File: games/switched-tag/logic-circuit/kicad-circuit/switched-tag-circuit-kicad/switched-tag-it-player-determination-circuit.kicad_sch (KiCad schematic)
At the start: 16 parts

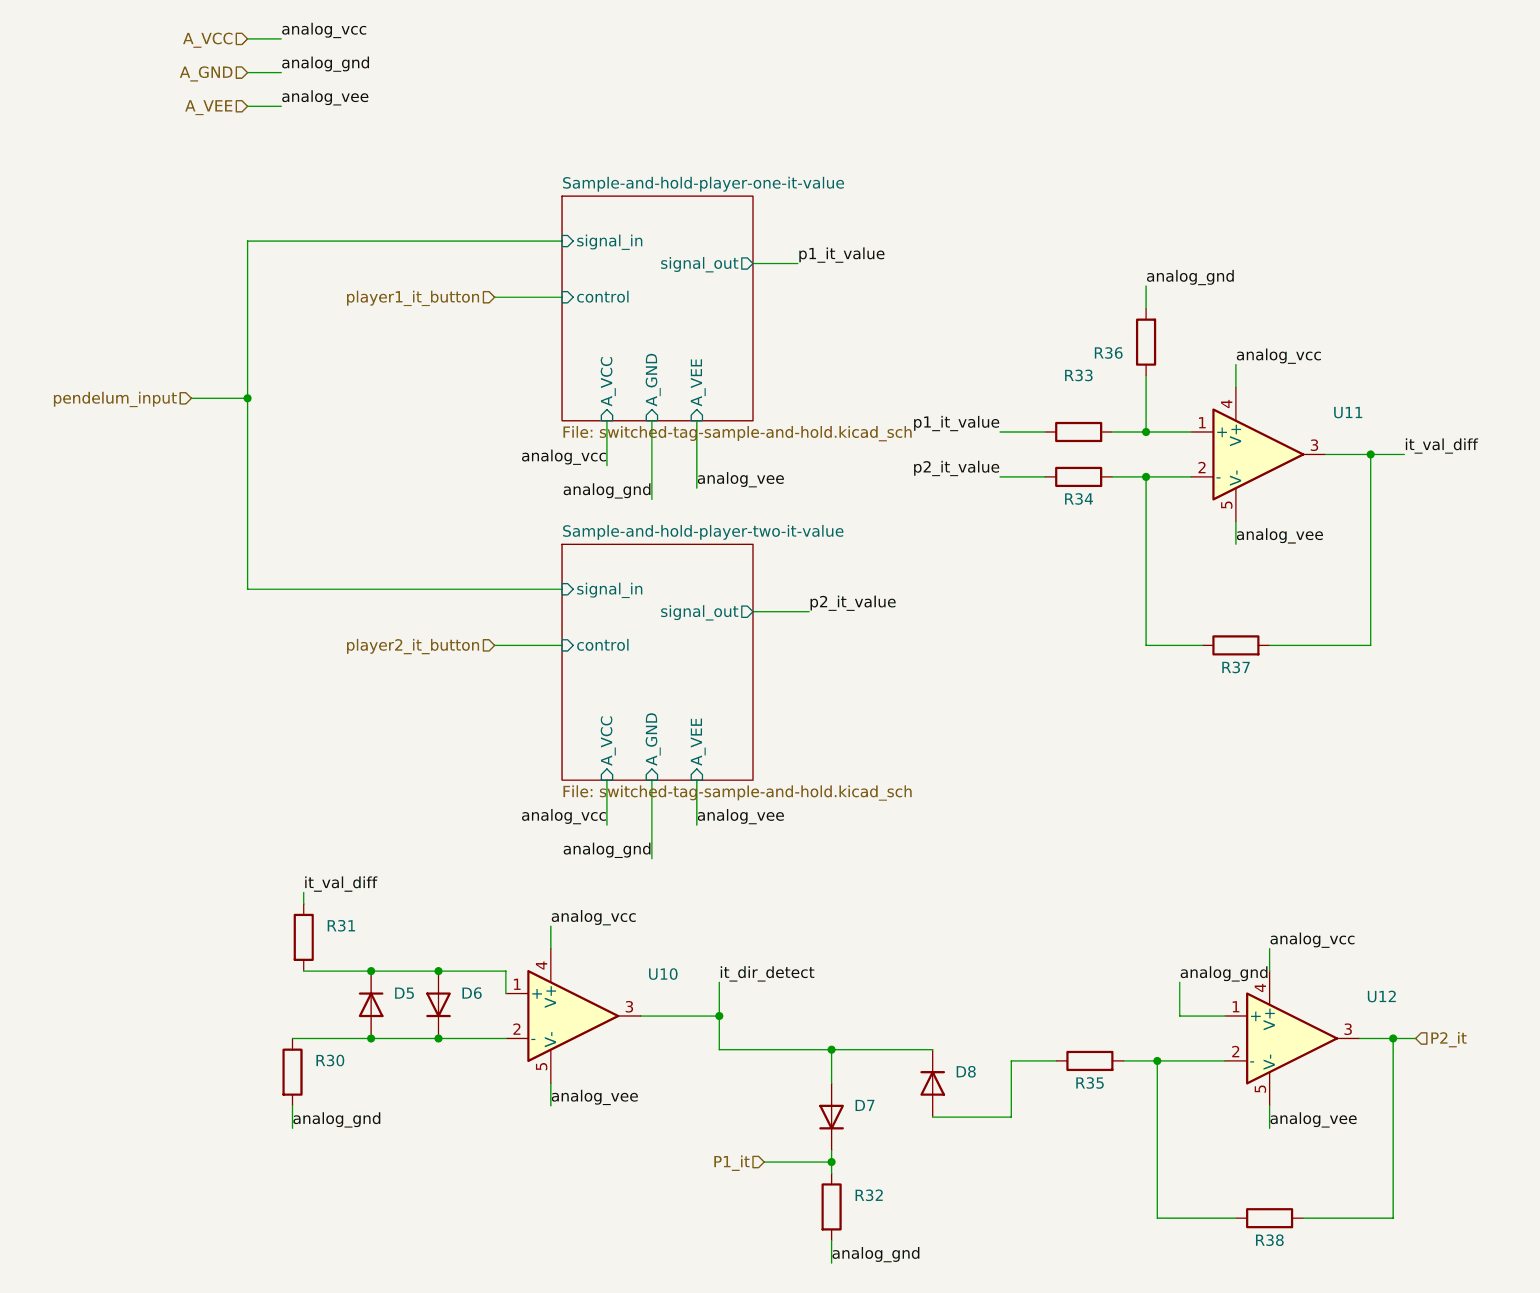
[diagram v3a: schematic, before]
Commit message: Updated kicad circuit. The kicad sim and ltspice do not match up well. Need to fix.
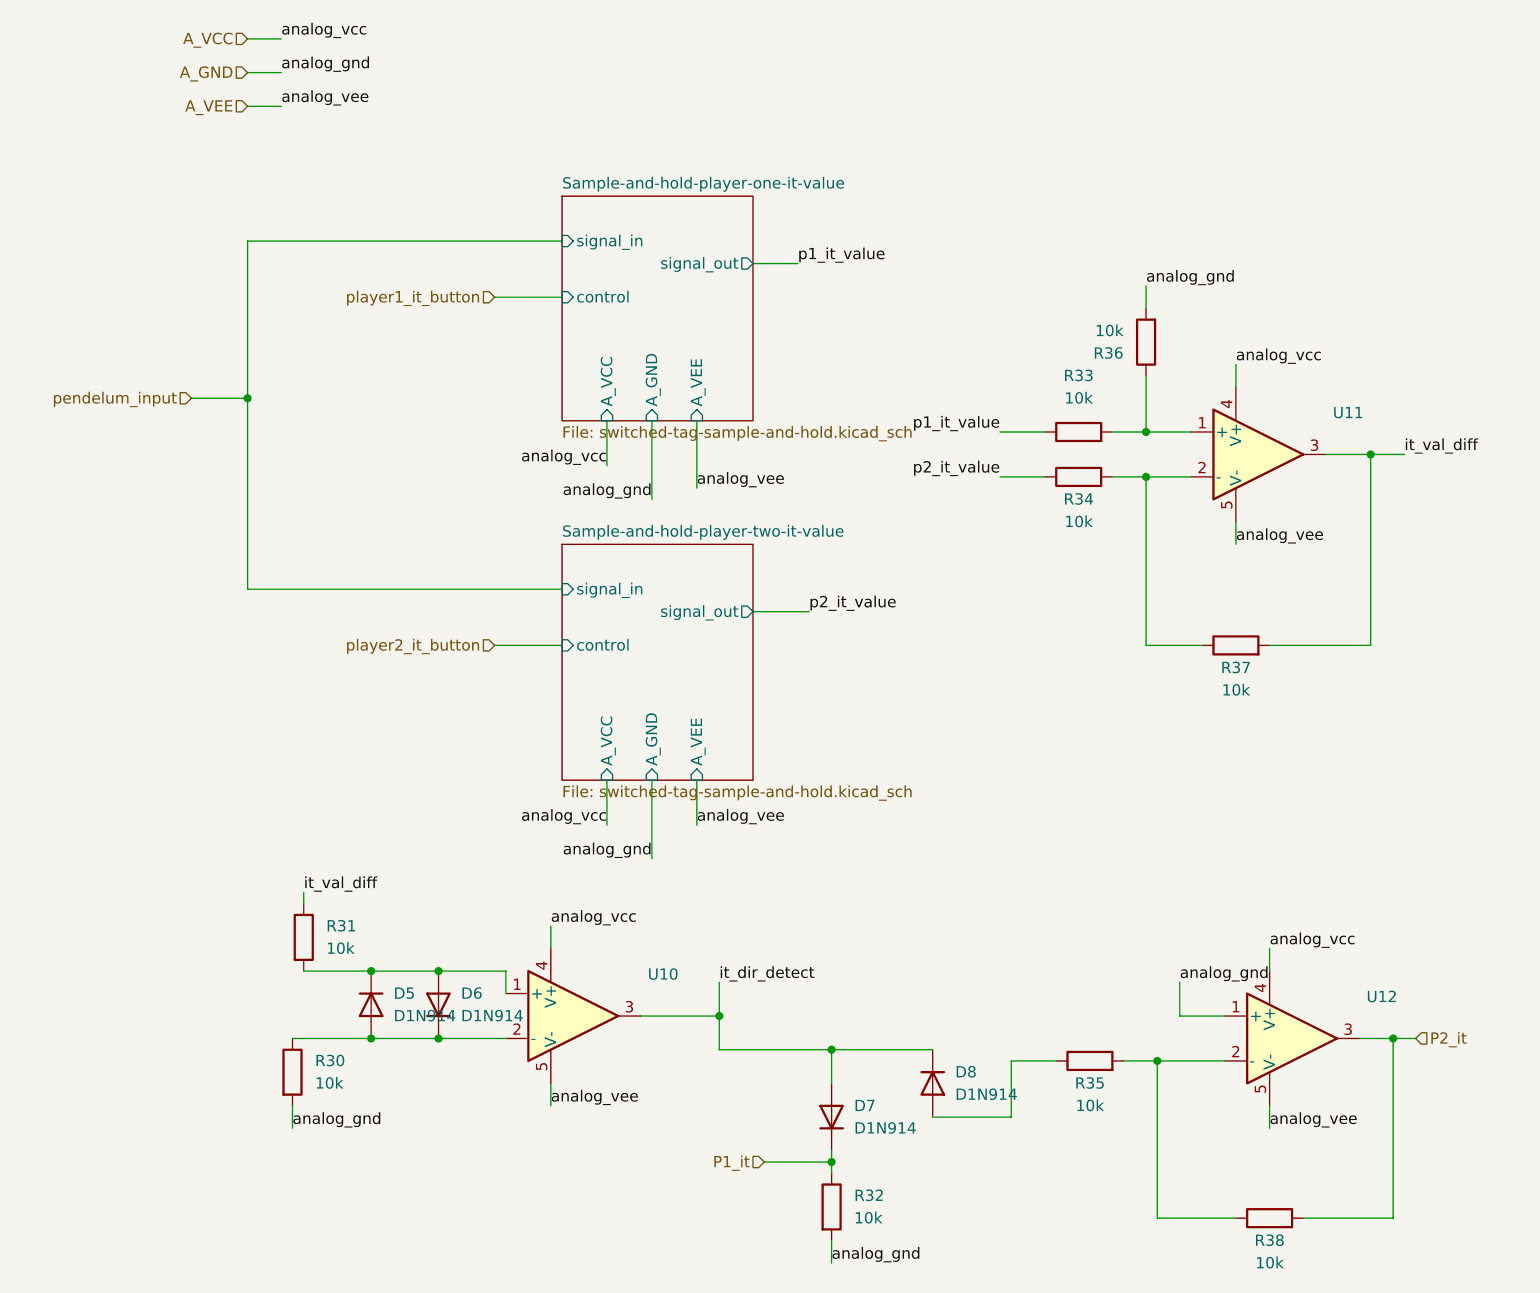
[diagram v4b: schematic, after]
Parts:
- D5, D6, D7, D8: value (none) -> D1N914
- R30, R31, R32, R33, R34, R35, R36, R37, R38: value (none) -> 10k
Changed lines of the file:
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@@
     (in_bom yes) (on_board yes) (fields_autoplaced)
     (property "Reference" "R33" (id 0) (at 132.08 72.39 90))
-    (property "Value" "" (id 1) (at 132.08 74.93 90))
+    (property "Value" "10k" (id 1) (at 132.08 74.93 90))
     (property "Footprint" "" (id 2) (at 132.08 80.518 90)
       (effects (font (size 1.27 1.27)) hide)
@@
       (effects (font (size 1.27 1.27)) (justify left))
     )
-    (property "Value" "" (id 1) (at 118.11 153.6699 90)
+    (property "Value" "D1N914" (id 1) (at 118.11 153.6699 90)
       (effects (font (size 1.27 1.27)) (justify left))
     )
@@
       (effects (font (size 1.27 1.27)) hide)
     )
-    (property "Datasheet" "~" (id 3) (at 115.57 152.4 0)
+    (property "Datasheet" "1n914" (id 3) (at 115.57 152.4 0)
       (effects (font (size 1.27 1.27)) hide)
     )
@@
       (effects (font (size 1.27 1.27)) (justify right))
     )
-    (property "Value" "" (id 1) (at 106.68 157.4799 90)
+    (property "Value" "D1N914" (id 1) (at 106.68 157.4799 90)
       (effects (font (size 1.27 1.27)) (justify right))
     )
@@
       (effects (font (size 1.27 1.27)) hide)
     )
-    (property "Datasheet" "~" (id 3) (at 104.14 156.21 0)
+    (property "Datasheet" "1n914" (id 3) (at 104.14 156.21 0)
       (effects (font (size 1.27 1.27)) hide)
     )
@@
       (effects (font (size 1.27 1.27)) (justify left))
     )
-    (property "Value" "" (id 1) (at 46.99 137.1599 0)
+    (property "Value" "10k" (id 1) (at 46.99 137.1599 0)
       (effects (font (size 1.27 1.27)) (justify left))
     )
@@
       (effects (font (size 1.27 1.27)) (justify left))
     )
-    (property "Value" "" (id 1) (at 54.61 144.7799 90)
+    (property "Value" "D1N914" (id 1) (at 54.61 144.7799 90)
       (effects (font (size 1.27 1.27)) (justify left))
     )
@@
       (effects (font (size 1.27 1.27)) (justify left))
     )
-    (property "Value" "" (id 1) (at 106.68 167.6399 0)
+    (property "Value" "10k" (id 1) (at 106.68 167.6399 0)
       (effects (font (size 1.27 1.27)) (justify left))
     )
@@
       (effects (font (size 1.27 1.27)) (justify left))
     )
-    (property "Value" "" (id 1) (at 45.72 152.3999 0)
+    (property "Value" "10k" (id 1) (at 45.72 152.3999 0)
       (effects (font (size 1.27 1.27)) (justify left))
     )
@@
     (in_bom yes) (on_board yes)
     (property "Reference" "R37" (id 0) (at 149.86 105.41 90))
-    (property "Value" "" (id 1) (at 149.86 107.95 90))
+    (property "Value" "10k" (id 1) (at 149.86 107.95 90))
     (property "Footprint" "" (id 2) (at 149.86 104.648 90)
       (effects (font (size 1.27 1.27)) hide)
@@
     (in_bom yes) (on_board yes)
     (property "Reference" "R34" (id 0) (at 132.08 86.36 90))
-    (property "Value" "" (id 1) (at 132.08 88.9 90))
+    (property "Value" "10k" (id 1) (at 132.08 88.9 90))
     (property "Footprint" "" (id 2) (at 132.08 85.598 90)
       (effects (font (size 1.27 1.27)) hide)
@@
     (in_bom yes) (on_board yes)
     (property "Reference" "R35" (id 0) (at 133.35 152.4 90))
-    (property "Value" "" (id 1) (at 133.35 154.94 90))
+    (property "Value" "10k" (id 1) (at 133.35 154.94 90))
     (property "Footprint" "" (id 2) (at 133.35 151.638 90)
       (effects (font (size 1.27 1.27)) hide)
@@
       (effects (font (size 1.27 1.27)) (justify right))
     )
-    (property "Value" "" (id 1) (at 62.23 144.7799 90)
+    (property "Value" "D1N914" (id 1) (at 62.23 144.7799 90)
       (effects (font (size 1.27 1.27)) (justify right))
     )
@@
       (effects (font (size 1.27 1.27)) hide)
     )
-    (property "Datasheet" "~" (id 3) (at 59.69 143.51 0)
+    (property "Datasheet" "1n914" (id 3) (at 59.69 143.51 0)
       (effects (font (size 1.27 1.27)) hide)
     )
@@
     (in_bom yes) (on_board yes)
     (property "Reference" "R38" (id 0) (at 153.67 170.18 90))
-    (property "Value" "" (id 1) (at 153.67 172.72 90))
+    (property "Value" "10k" (id 1) (at 153.67 172.72 90))
     (property "Footprint" "" (id 2) (at 153.67 169.418 90)
       (effects (font (size 1.27 1.27)) hide)
@@
       (effects (font (size 1.27 1.27)) (justify left))
     )
-    (property "Value" "" (id 1) (at 137.16 67.3101 0)
-      (effects (font (size 1.27 1.27)) (justify left))
-    )
+    (property "Value" "10k" (id 1) (at 137.16 67.3101 0)
+      (effects (font (size 1.27 1.27)) (justify left))
+    )

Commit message: Added some prep work for console hardware.
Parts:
- D5, D6, D7, D8: value D1N914 -> (none); Spice_Lib_File /home/pab/Inventions/analog-circuit-game-console/ms-circuit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 -> ../../../../../spice-models/1N914.lib
- R30, R31, R32, R33, R34, R35, R36, R37, R38: value 10k -> (none)
- U10, U11, U12: Spice_Lib_File /home/pab/Inventions/analog-circuit-game-console/ms-circuit-video-games/spice-models/ada4692.mod -> /home/pab/Inventions/analog-circuit-game-console/ms-circuit-video-games/spice-models/lmx58_lm2904.lib; Spice_Model ADA4692 -> LMX58_LM2904
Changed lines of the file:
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@@
       (effects (font (size 1.27 1.27)) (justify left) hide)
     )
-    (property "Spice_Model" "ADA4692" (id 6) (at 74.93 144.78 0)
-      (effects (font (size 1.27 1.27)) hide)
-    )
-    (property "Spice_Lib_File" "/home/pab/Inventions/analog-circuit-game-console/ms-circuit-video-games/spice-models/ada4692.mod" (id 7) (at 74.93 144.78 0)
+    (property "Spice_Model" "LMX58_LM2904" (id 6) (at 74.93 144.78 0)
+      (effects (font (size 1.27 1.27)) hide)
+    )
+    (property "Spice_Lib_File" "/home/pab/Inventions/analog-circuit-game-console/ms-circuit-video-games/spice-models/lmx58_lm2904.lib" (id 7) (at 74.93 144.78 0)
       (effects (font (size 1.27 1.27)) hide)
     )
@@
     (in_bom yes) (on_board yes) (fields_autoplaced)
     (property "Reference" "R33" (id 0) (at 132.08 72.39 90))
-    (property "Value" "10k" (id 1) (at 132.08 74.93 90))
+    (property "Value" "" (id 1) (at 132.08 74.93 90))
     (property "Footprint" "" (id 2) (at 132.08 80.518 90)
       (effects (font (size 1.27 1.27)) hide)
@@
       (effects (font (size 1.27 1.27)) (justify left))
     )
-    (property "Value" "D1N914" (id 1) (at 118.11 153.6699 90)
+    (property "Value" "" (id 1) (at 118.11 153.6699 90)
       (effects (font (size 1.27 1.27)) (justify left))
     )
@@
       (effects (font (size 1.27 1.27)) hide)
     )
-    (property "Spice_Lib_File" "/home/pab/Inventions/analog-circuit-game-console/ms-circuit-video-games/spice-models/1N914.lib" (id 4) (at 115.57 152.4 0)
+    (property "Spice_Lib_File" "../../../../../spice-models/1N914.lib" (id 4) (at 115.57 152.4 0)
       (effects (font (size 1.27 1.27)) hide)
     )
@@
       (effects (font (size 1.27 1.27)) (justify right))
     )
-    (property "Value" "D1N914" (id 1) (at 106.68 157.4799 90)
+    (property "Value" "" (id 1) (at 106.68 157.4799 90)
       (effects (font (size 1.27 1.27)) (justify right))
     )
@@
       (effects (font (size 1.27 1.27)) hide)
     )
-    (property "Spice_Lib_File" "/home/pab/Inventions/analog-circuit-game-console/ms-circuit-video-games/spice-models/1N914.lib" (id 4) (at 104.14 156.21 0)
+    (property "Spice_Lib_File" "../../../../../spice-models/1N914.lib" (id 4) (at 104.14 156.21 0)
       (effects (font (size 1.27 1.27)) hide)
     )
@@
       (effects (font (size 1.27 1.27)) (justify left) hide)
     )
-    (property "Spice_Model" "ADA4692" (id 6) (at 156.21 147.32 0)
-      (effects (font (size 1.27 1.27)) hide)
-    )
-    (property "Spice_Lib_File" "/home/pab/Inventions/analog-circuit-game-console/ms-circuit-video-games/spice-models/ada4692.mod" (id 7) (at 156.21 147.32 0)
+    (property "Spice_Model" "LMX58_LM2904" (id 6) (at 156.21 147.32 0)
+      (effects (font (size 1.27 1.27)) hide)
+    )
+    (property "Spice_Lib_File" "/home/pab/Inventions/analog-circuit-game-console/ms-circuit-video-games/spice-models/lmx58_lm2904.lib" (id 7) (at 156.21 147.32 0)
       (effects (font (size 1.27 1.27)) hide)
     )
@@
       (effects (font (size 1.27 1.27)) (justify left))
     )
-    (property "Value" "10k" (id 1) (at 46.99 137.1599 0)
+    (property "Value" "" (id 1) (at 46.99 137.1599 0)
       (effects (font (size 1.27 1.27)) (justify left))
     )
@@
       (effects (font (size 1.27 1.27)) (justify left))
     )
-    (property "Value" "D1N914" (id 1) (at 54.61 144.7799 90)
+    (property "Value" "" (id 1) (at 54.61 144.7799 90)
       (effects (font (size 1.27 1.27)) (justify left))
     )
@@
       (effects (font (size 1.27 1.27)) hide)
     )
-    (property "Spice_Lib_File" "/home/pab/Inventions/analog-circuit-game-console/ms-circuit-video-games/spice-models/1N914.lib" (id 4) (at 52.07 143.51 0)
+    (property "Spice_Lib_File" "../../../../../spice-models/1N914.lib" (id 4) (at 52.07 143.51 0)
       (effects (font (size 1.27 1.27)) hide)
     )
@@
       (effects (font (size 1.27 1.27)) (justify left))
     )
-    (property "Value" "10k" (id 1) (at 106.68 167.6399 0)
+    (property "Value" "" (id 1) (at 106.68 167.6399 0)
       (effects (font (size 1.27 1.27)) (justify left))
     )
@@
       (effects (font (size 1.27 1.27)) (justify left) hide)
     )
-    (property "Spice_Model" "ADA4692" (id 6) (at 152.4 81.28 0)
-      (effects (font (size 1.27 1.27)) hide)
-    )
-    (property "Spice_Lib_File" "/home/pab/Inventions/analog-circuit-game-console/ms-circuit-video-games/spice-models/ada4692.mod" (id 7) (at 152.4 81.28 0)
+    (property "Spice_Model" "LMX58_LM2904" (id 6) (at 152.4 81.28 0)
+      (effects (font (size 1.27 1.27)) hide)
+    )
+    (property "Spice_Lib_File" "/home/pab/Inventions/analog-circuit-game-console/ms-circuit-video-games/spice-models/lmx58_lm2904.lib" (id 7) (at 152.4 81.28 0)
       (effects (font (size 1.27 1.27)) hide)
     )
@@
       (effects (font (size 1.27 1.27)) (justify left))
     )
-    (property "Value" "10k" (id 1) (at 45.72 152.3999 0)
+    (property "Value" "" (id 1) (at 45.72 152.3999 0)
       (effects (font (size 1.27 1.27)) (justify left))
     )
@@
     (in_bom yes) (on_board yes)
     (property "Reference" "R37" (id 0) (at 149.86 105.41 90))
-    (property "Value" "10k" (id 1) (at 149.86 107.95 90))
+    (property "Value" "" (id 1) (at 149.86 107.95 90))
     (property "Footprint" "" (id 2) (at 149.86 104.648 90)
       (effects (font (size 1.27 1.27)) hide)
@@
     (in_bom yes) (on_board yes)
     (property "Reference" "R34" (id 0) (at 132.08 86.36 90))
-    (property "Value" "10k" (id 1) (at 132.08 88.9 90))
+    (property "Value" "" (id 1) (at 132.08 88.9 90))
     (property "Footprint" "" (id 2) (at 132.08 85.598 90)
       (effects (font (size 1.27 1.27)) hide)
@@
     (in_bom yes) (on_board yes)
     (property "Reference" "R35" (id 0) (at 133.35 152.4 90))
-    (property "Value" "10k" (id 1) (at 133.35 154.94 90))
+    (property "Value" "" (id 1) (at 133.35 154.94 90))
     (property "Footprint" "" (id 2) (at 133.35 151.638 90)
       (effects (font (size 1.27 1.27)) hide)
@@
       (effects (font (size 1.27 1.27)) (justify right))
     )
-    (property "Value" "D1N914" (id 1) (at 62.23 144.7799 90)
+    (property "Value" "" (id 1) (at 62.23 144.7799 90)
       (effects (font (size 1.27 1.27)) (justify right))
     )
@@
       (effects (font (size 1.27 1.27)) hide)
     )
-    (property "Spice_Lib_File" "/home/pab/Inventions/analog-circuit-game-console/ms-circuit-video-games/spice-models/1N914.lib" (id 4) (at 59.69 143.51 0)
+    (property "Spice_Lib_File" "../../../../../spice-models/1N914.lib" (id 4) (at 59.69 143.51 0)
       (effects (font (size 1.27 1.27)) hide)
     )
@@
     (in_bom yes) (on_board yes)
     (property "Reference" "R38" (id 0) (at 153.67 170.18 90))
-    (property "Value" "10k" (id 1) (at 153.67 172.72 90))
+    (property "Value" "" (id 1) (at 153.67 172.72 90))
     (property "Footprint" "" (id 2) (at 153.67 169.418 90)
       (effects (font (size 1.27 1.27)) hide)
@@
       (effects (font (size 1.27 1.27)) (justify left))
     )
-    (property "Value" "10k" (id 1) (at 137.16 67.3101 0)
-      (effects (font (size 1.27 1.27)) (justify left))
-    )
+    (property "Value" "" (id 1) (at 137.16 67.3101 0)
+      (effects (font (size 1.27 1.27)) (justify left))
+    )

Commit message: Saving progress.
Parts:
- U10, U11, U12: Spice_Lib_File /home/pab/Inventions/analog-circuit-game-console/ms-circuit-video-games/spice-models/lmx58_lm2904.lib -> /home/pab/Inventions/analog-circuit-game-console/ms-circuit-video-games/spice-models/ad8031.mod; Spice_Model LMX58_LM2904 -> AD8031
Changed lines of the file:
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@@
       (effects (font (size 1.27 1.27)) (justify left) hide)
     )
-    (property "Spice_Model" "LMX58_LM2904" (id 6) (at 74.93 144.78 0)
-      (effects (font (size 1.27 1.27)) hide)
-    )
-    (property "Spice_Lib_File" "/home/pab/Inventions/analog-circuit-game-console/ms-circuit-video-games/spice-models/lmx58_lm2904.lib" (id 7) (at 74.93 144.78 0)
+    (property "Spice_Model" "AD8031" (id 6) (at 74.93 144.78 0)
+      (effects (font (size 1.27 1.27)) hide)
+    )
+    (property "Spice_Lib_File" "/home/pab/Inventions/analog-circuit-game-console/ms-circuit-video-games/spice-models/ad8031.mod" (id 7) (at 74.93 144.78 0)
       (effects (font (size 1.27 1.27)) hide)
     )
@@
       (effects (font (size 1.27 1.27)) (justify left) hide)
     )
-    (property "Spice_Model" "LMX58_LM2904" (id 6) (at 156.21 147.32 0)
-      (effects (font (size 1.27 1.27)) hide)
-    )
-    (property "Spice_Lib_File" "/home/pab/Inventions/analog-circuit-game-console/ms-circuit-video-games/spice-models/lmx58_lm2904.lib" (id 7) (at 156.21 147.32 0)
+    (property "Spice_Model" "AD8031" (id 6) (at 156.21 147.32 0)
+      (effects (font (size 1.27 1.27)) hide)
+    )
+    (property "Spice_Lib_File" "/home/pab/Inventions/analog-circuit-game-console/ms-circuit-video-games/spice-models/ad8031.mod" (id 7) (at 156.21 147.32 0)
       (effects (font (size 1.27 1.27)) hide)
     )
@@
       (effects (font (size 1.27 1.27)) (justify left) hide)
     )
-    (property "Spice_Model" "LMX58_LM2904" (id 6) (at 152.4 81.28 0)
-      (effects (font (size 1.27 1.27)) hide)
-    )
-    (property "Spice_Lib_File" "/home/pab/Inventions/analog-circuit-game-console/ms-circuit-video-games/spice-models/lmx58_lm2904.lib" (id 7) (at 152.4 81.28 0)
-      (effects (font (size 1.27 1.27)) hide)
-    )
+    (property "Spice_Model" "AD8031" (id 6) (at 152.4 81.28 0)
+      (effects (font (size 1.27 1.27)) hide)
+    )
+    (property "Spice_Lib_File" "/home/pab/Inventions/analog-circuit-game-console/ms-circuit-video-games/spice-models/ad8031.mod" (id 7) (at 152.4 81.28 0)
+      (effects (font (size 1.27 1.27)) hide)
+    )
